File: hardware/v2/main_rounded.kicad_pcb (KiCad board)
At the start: 2 copper layers, 129.5 x 50.8 mm, 39 parts, among them J2 Ext, J3 uSD, J4 TP4056, J6 AudioJack, Q1 IRLML6401, SW1 Up, SW10 Start, SW11 Power, SW12 Reset, SW2 Down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

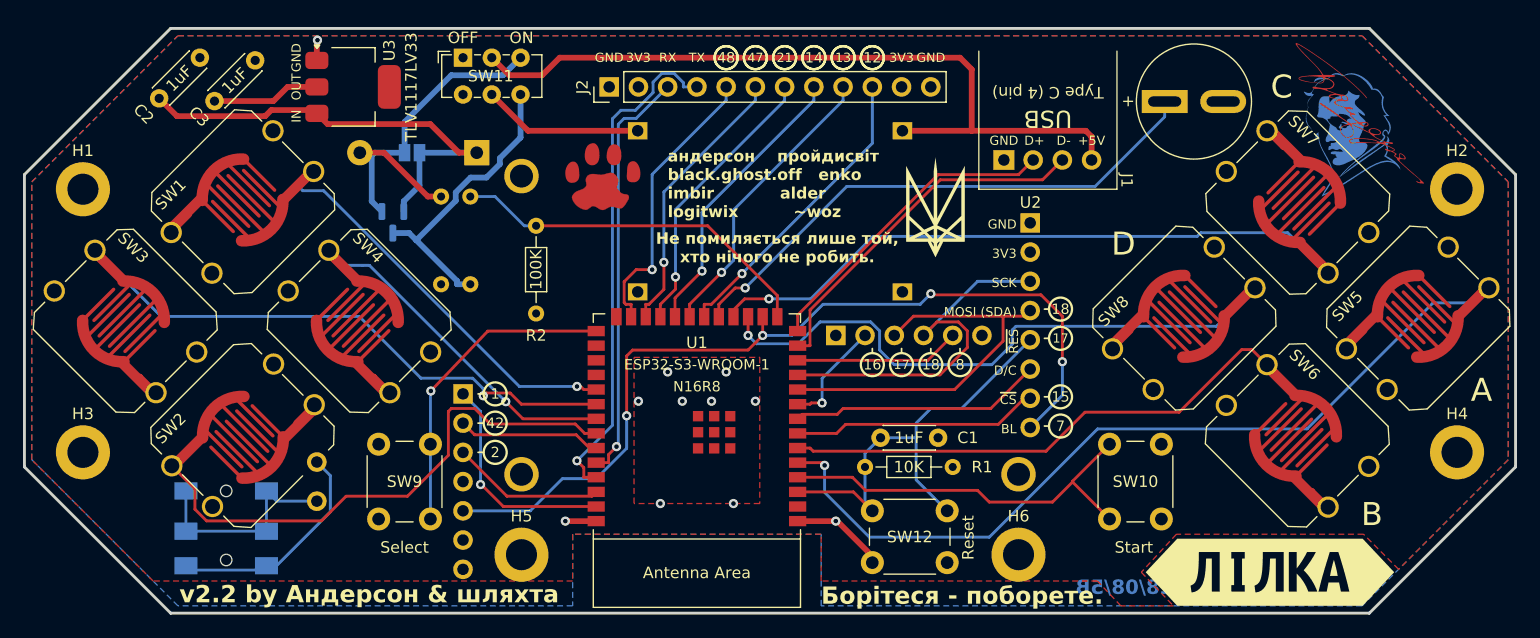
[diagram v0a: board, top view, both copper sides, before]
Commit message: hardware: add rounded tracks, cleanup duplicate/hidden tracks, move uSD card away from display connector
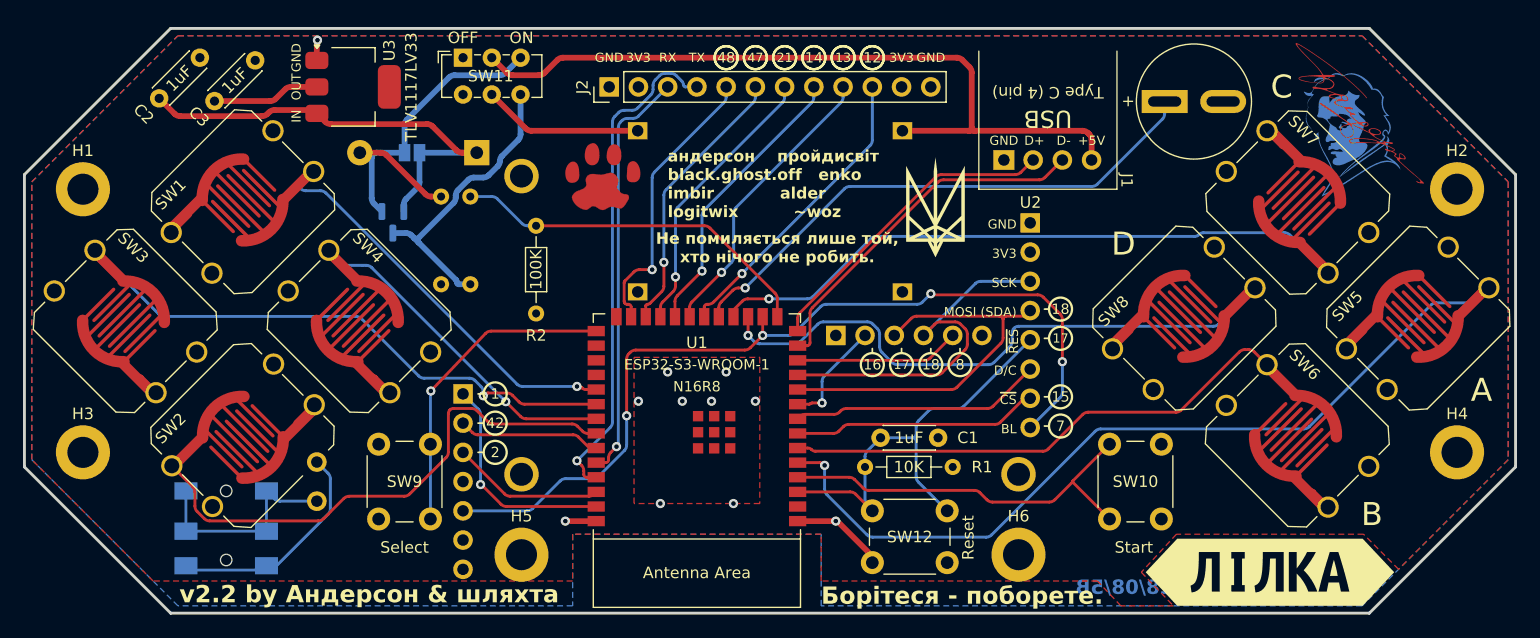
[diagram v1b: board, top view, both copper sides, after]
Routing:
- net A: track 74.9 -> 74.4 mm
- net TX: track 44.0 -> 43.4 mm

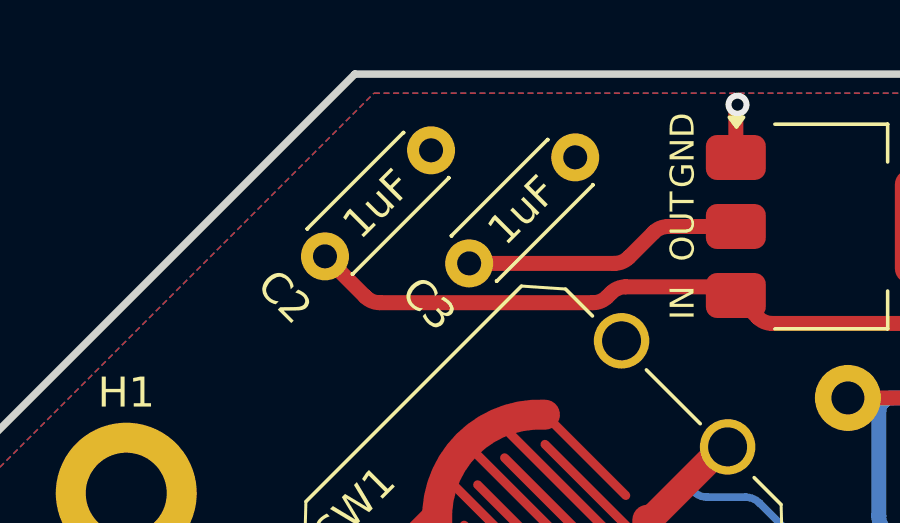
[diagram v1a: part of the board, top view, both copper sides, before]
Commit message: Update C2, C3 value from 1uF to 10uF on main{,_rounded}.kicad_pcb
Docs were updated on Jan 2 to these values. Assuming it was correct.

Link: 7412343db23f ("Fix component values and count")
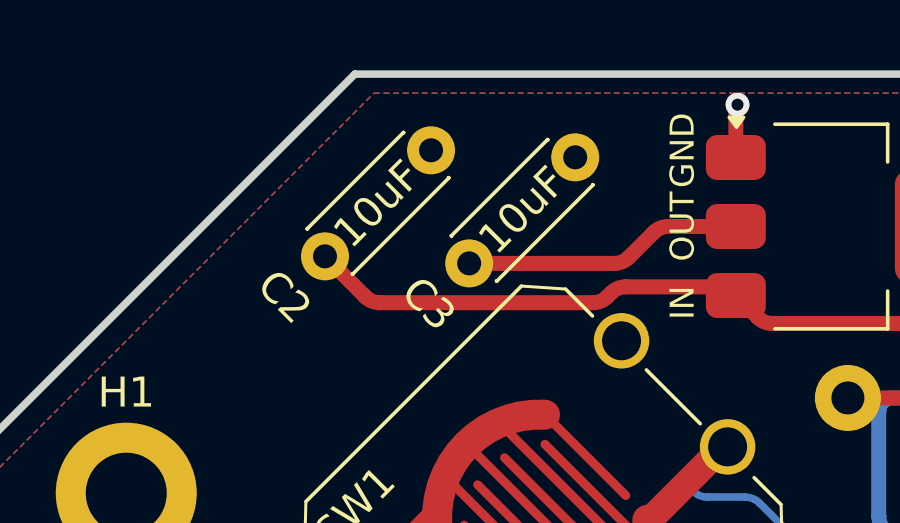
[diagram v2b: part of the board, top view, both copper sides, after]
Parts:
- C2, C3: value 1uF -> 10uF
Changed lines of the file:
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@@
 			)
 		)
-		(property "Value" "1uF"
+		(property "Value" "10uF"
 			(at 2.46 0 45)
 			(layer "F.SilkS")
@@
 			)
 		)
-		(property "Value" "1uF"
+		(property "Value" "10uF"
 			(at 2.5 0 45)
 			(layer "F.SilkS")
